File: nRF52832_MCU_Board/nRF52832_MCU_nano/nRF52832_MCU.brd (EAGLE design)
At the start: 55.7 x 22.9 mm, 57 parts, among them J1 TSW-103-02-S-S, J2 TSW-116-02-S-S, J3 TSW-116-02-S-S, J4 TSW-103-02-S-S, J5 MICROUSB, J6 DEBUG_CONNECTOR, J7 FPC_05P-RA-SMD, J8 MM8130-2600, U1 NRF52832, U2 TLV1117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

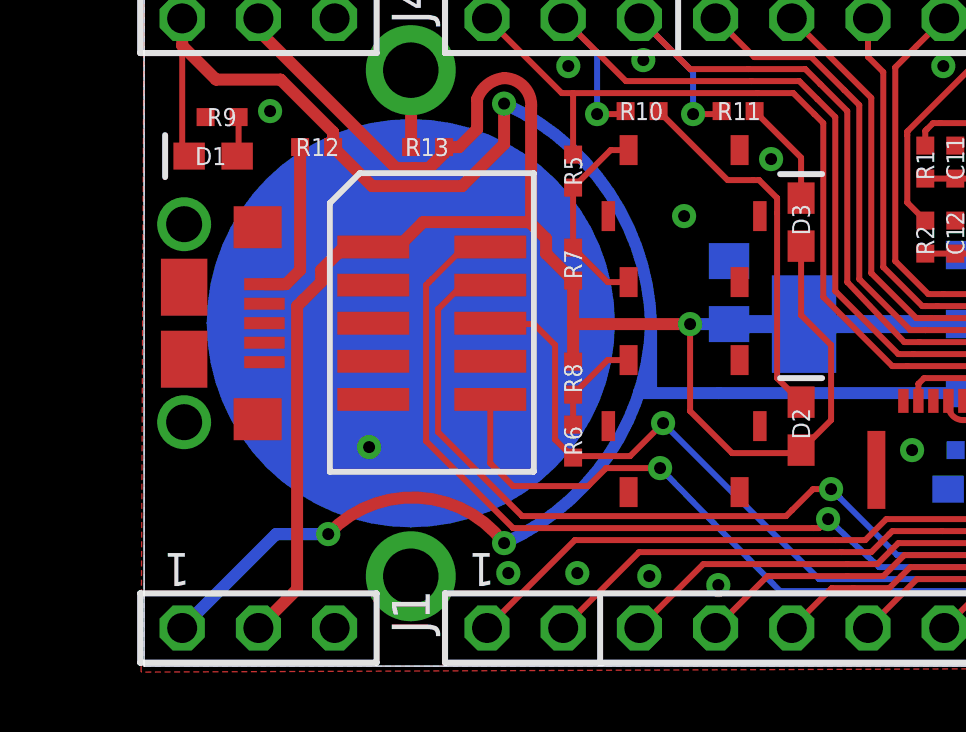
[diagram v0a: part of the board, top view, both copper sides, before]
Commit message: Added some vias
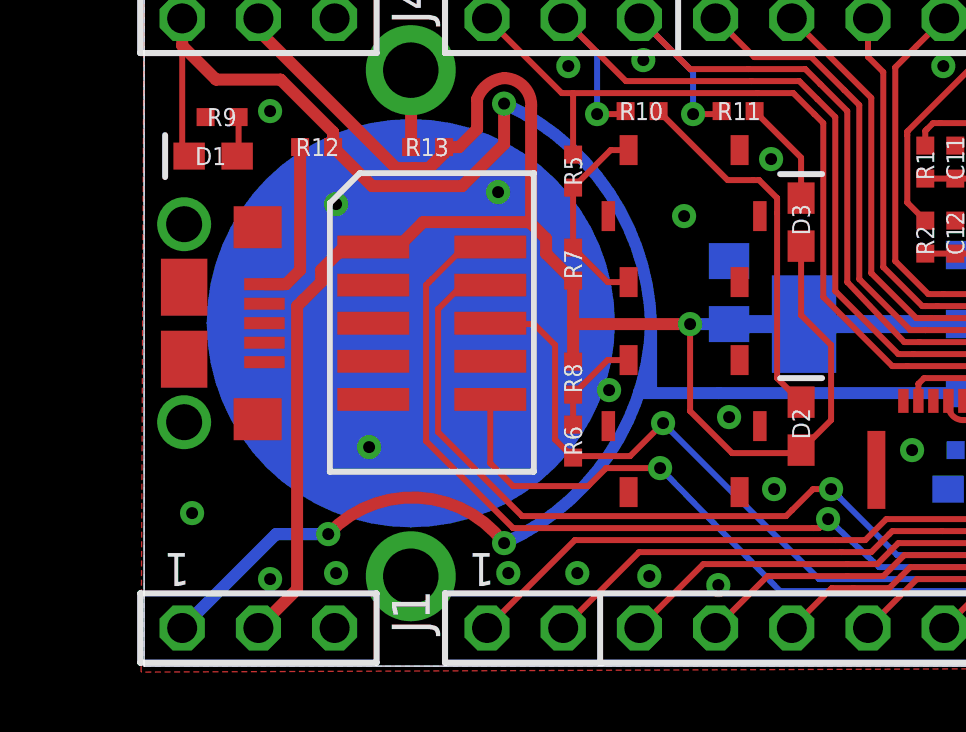
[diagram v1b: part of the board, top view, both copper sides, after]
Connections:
- net N$6: no longer U$5.2
- net VDD_P3V3_BATT: no longer BATT1.3
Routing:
- net GND: vias 67 -> 76
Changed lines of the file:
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@@
 <wire x1="8.89" y1="18.034" x2="15.494" y2="11.43" width="0.4" layer="16" curve="-90"/>
 <wire x1="15.494" y1="11.43" x2="8.89" y2="4.826" width="0.4" layer="16" curve="-90"/>
+<via x="11.8" y="15.8" extent="1-16" drill="0.4" diameter="0.8"/>
+<via x="6.4" y="15.4" extent="1-16" drill="0.4" diameter="0.8"/>
+<via x="1.6" y="5.1" extent="1-16" drill="0.4" diameter="0.8"/>
+<via x="4.2" y="2.9" extent="1-16" drill="0.4" diameter="0.8"/>
+<via x="6.4" y="3.1" extent="1-16" drill="0.4" diameter="0.8"/>
+<via x="15.5" y="9.2" extent="1-16" drill="0.4" diameter="0.8"/>
+<via x="19.5" y="8.3" extent="1-16" drill="0.4" diameter="0.8"/>
+<via x="21" y="5.9" extent="1-16" drill="0.4" diameter="0.8"/>
+<via x="30" y="18.6" extent="1-16" drill="0.4"/>
 <wire x1="8.89" y1="11.43" x2="7.64" y2="11.43" width="0" layer="19" extent="1-16"/>
-<wire x1="15.475" y1="8" x2="15.494" y2="11.43" width="0" layer="19" extent="1-16"/>
 </signal>
 <signal name="DEC1">
@@
 </signal>
 <signal name="N$6">
-<contactref element="U$5" pad="2"/>
 <contactref element="R8" pad="1"/>
 <contactref element="U$5" pad="1"/>
@@
 <wire x1="15.45" y1="10.2" x2="16.15" y2="10.2" width="0.2" layer="1"/>
 <wire x1="14.3" y1="9.05" x2="14.3" y2="8.05" width="0.2" layer="1"/>
-<wire x1="14.3" y1="8.05" x2="16.15" y2="5.8" width="0" layer="19" extent="1-1"/>
 </signal>
 <signal name="N$7">
@@
 <contactref element="BATT1" pad="2"/>
 <contactref element="R13" pad="1"/>
-<contactref element="BATT1" pad="3"/>
 <wire x1="8.9" y1="17.3" x2="8.9" y2="19.855" width="0.4" layer="1"/>
 <wire x1="8.9" y1="19.855" x2="8.89" y2="19.865" width="0.4" layer="1"/>
-<wire x1="8.89" y1="2.995" x2="8.9" y2="17.3" width="0" layer="19" extent="1-1"/>
-</signal>
-<signal name="N$15">
-<via x="30" y="18.6" extent="1-16" drill="0.4"/>
 </signal>
 </signals>

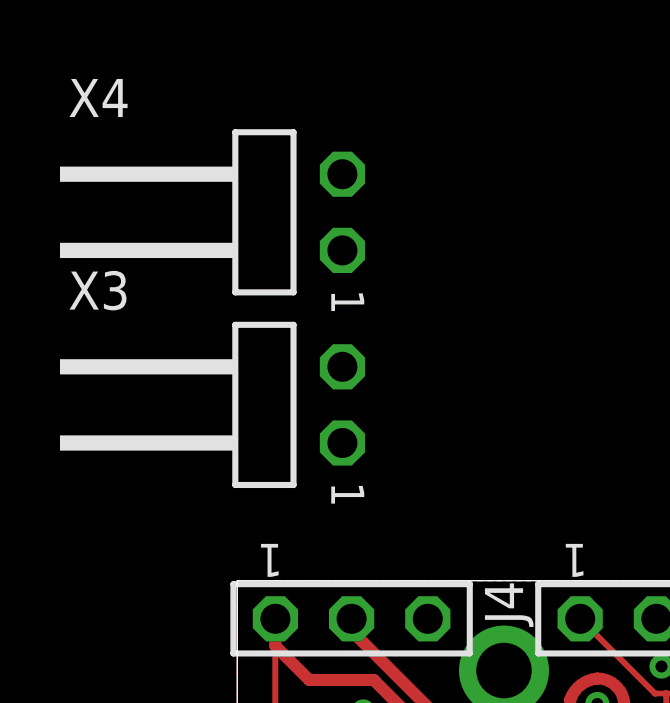
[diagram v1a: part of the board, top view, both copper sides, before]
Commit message: Cleaned up schematic
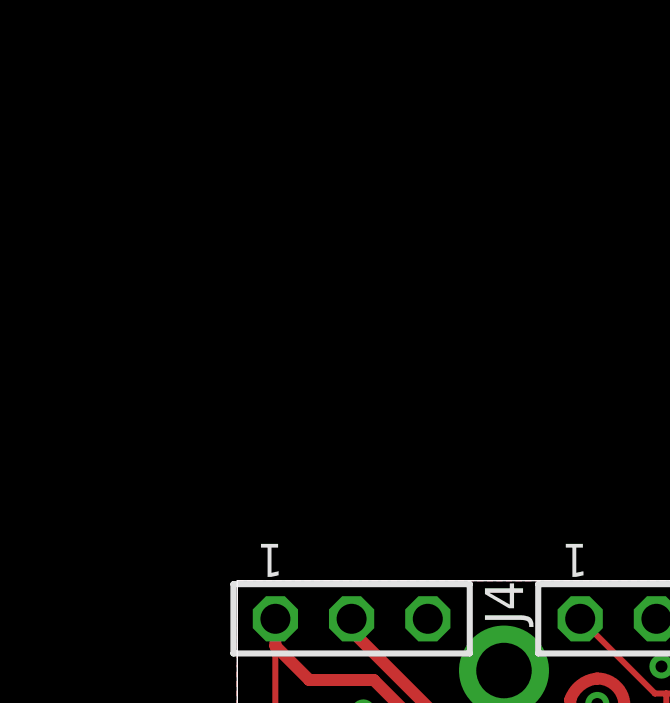
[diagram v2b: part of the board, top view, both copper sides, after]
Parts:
- removed X3, X4: TSW-102-02-S-S-RA, con-samtec:TSW-102-02-S-S-RA
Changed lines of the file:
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@@
 </element>
 <element name="J5" library="Nordic_misc" package="USB-MICRO-B-RA-SMD-PIP" value="MICROUSB" x="4.01" y="11.43"/>
-<element name="X3" library="con-samtec" package="TSW-102-02-S-S-RA" value="TSW-102-02-S-S-RA" x="1.98" y="28.72" rot="R270">
-<attribute name="OC_FARNELL" value="unknown" x="1.98" y="28.72" size="1.778" layer="27" rot="R270" display="off"/>
-<attribute name="MF" value="" x="1.98" y="28.72" size="1.778" layer="27" rot="R270" display="off"/>
-<attribute name="MPN" value="" x="1.98" y="28.72" size="1.778" layer="27" rot="R270" display="off"/>
-<attribute name="OC_NEWARK" value="unknown" x="1.98" y="28.72" size="1.778" layer="27" rot="R270" display="off"/>
-</element>
-<element name="X4" library="con-samtec" package="TSW-102-02-S-S-RA" value="TSW-102-02-S-S-RA" x="1.98" y="35.14" rot="R270">
-<attribute name="OC_FARNELL" value="unknown" x="1.98" y="35.14" size="1.778" layer="27" rot="R270" display="off"/>
-<attribute name="MF" value="" x="1.98" y="35.14" size="1.778" layer="27" rot="R270" display="off"/>
-<attribute name="MPN" value="" x="1.98" y="35.14" size="1.778" layer="27" rot="R270" display="off"/>
-<attribute name="OC_NEWARK" value="unknown" x="1.98" y="35.14" size="1.778" layer="27" rot="R270" display="off"/>
-</element>
 <element name="J1" library="con-samtec" package="TSW-103-02-S-S" value="TSW-103-02-S-S" x="3.81" y="1.27" rot="R180">
 <attribute name="OC_FARNELL" value="unknown" x="3.81" y="1.27" size="1.778" layer="27" rot="R180" display="off"/>
